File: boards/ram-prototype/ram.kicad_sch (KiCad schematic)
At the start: 29 parts, among them J1 SRAM_Bus

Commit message: Fix a bunch of issues
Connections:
- net D0: now also R1.1; no longer R4.1
- net D1: now also R2.1; no longer R5.1
- net D2: now also R3.1; no longer R6.1
- net D3: now also R4.1; no longer R7.1
- net D4: now also R5.1; no longer R8.1
- net D5: now also R6.1; no longer R9.1
- net D6: now also R7.1; no longer R10.1
- net D7: now also R8.1; no longer R11.1
- net GND: now also D11.2 (A), D14.2 (A), R11.2, R14.2
- net A0 renamed Address Decoder/A0
- net Address Decoder/A0: now also R9.1; no longer R1.1
- net A1 renamed Address Decoder/A1
- net Address Decoder/A1: now also R10.1; no longer R2.1
- net A2 renamed Address Decoder/A2
- net Address Decoder/A2: now also R11.1; no longer R3.1
- net nCE renamed Control Logic/nCE
- net nOE renamed Control Logic/nOE
- net nWE renamed Control Logic/nWE

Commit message: Clean up root
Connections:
- net D0: now also R4.1; no longer R1.1
- net D1: now also R5.1; no longer R2.1
- net D2: now also R6.1; no longer R3.1
- net D3: now also R7.1; no longer R4.1
- net D4: now also R8.1; no longer R5.1
- net D5: now also R9.1; no longer R6.1
- net D6: now also R10.1; no longer R7.1
- net D7: now also R11.1; no longer R8.1
- net GND: no longer D11.2 (A), D14.2 (A), R11.2, R14.2
- net Address Decoder/A0 renamed A0
- net A0: now also R1.1; no longer R9.1
- net Address Decoder/A1 renamed A1
- net A1: now also R2.1; no longer R10.1
- net Address Decoder/A2 renamed A2
- net A2: now also R3.1; no longer R11.1
- net Control Logic/nCE renamed nCE
- net Control Logic/nOE renamed nOE
- net Control Logic/nWE renamed nWE
- new net: D11.2 (A), R11.2
- new net: D14.2 (A), R14.2

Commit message: Continue with updates
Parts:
- removed J1: SRAM_Bus, symbol Connector_Generic:Conn_01x14
- added J1: SRAM_Bus, symbol Connector_Generic:Conn_01x16
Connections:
- net A0: now also J1.1 (Pin_1)
- net A1: now also J1.2 (Pin_2)
- net A2: now also J1.3 (Pin_3)
- net D0: now also J1.4 (Pin_4)
- net D1: now also J1.5 (Pin_5)
- net D2: now also J1.6 (Pin_6)
- net D3: now also J1.7 (Pin_7)
- net D4: now also J1.8 (Pin_8)
- net D5: now also J1.9 (Pin_9)
- net D6: now also J1.10 (Pin_10)
- net D7: now also J1.11 (Pin_11)
- net GND: now also J1.16 (Pin_16)
- net nCE: now also J1.12 (Pin_12)
- net nOE: now also J1.13 (Pin_13)
- net nWE: now also J1.14 (Pin_14)
- new net VCC: J1.15 (Pin_15)

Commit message: More reasonable top level designrout
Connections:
- net A0: now also J1.2 (Pin_2); no longer J1.1 (Pin_1)
- net A1: now also J1.3 (Pin_3); no longer J1.2 (Pin_2)
- net A2: now also J1.4 (Pin_4); no longer J1.3 (Pin_3)
- net D0: now also J1.5 (Pin_5); no longer J1.4 (Pin_4)
- net D1: now also J1.6 (Pin_6); no longer J1.5 (Pin_5)
- net D2: now also J1.7 (Pin_7); no longer J1.6 (Pin_6)
- net D3: now also J1.8 (Pin_8); no longer J1.7 (Pin_7)
- net D4: now also J1.9 (Pin_9); no longer J1.8 (Pin_8)
- net D5: now also J1.10 (Pin_10); no longer J1.9 (Pin_9)
- net D6: now also J1.11 (Pin_11); no longer J1.10 (Pin_10)
- net D7: now also J1.12 (Pin_12); no longer J1.11 (Pin_11)
- net GND: now also J1.1 (Pin_1); no longer J1.16 (Pin_16)
- net VCC: now also J1.16 (Pin_16); no longer J1.15 (Pin_15)
- net nCE: now also J1.13 (Pin_13); no longer J1.12 (Pin_12)
- net nOE: now also J1.14 (Pin_14); no longer J1.13 (Pin_13)
- net nWE: now also J1.15 (Pin_15); no longer J1.14 (Pin_14)

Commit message: Clean up root more and add more data
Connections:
- net A0: now also R14.1; no longer R1.1
- net A1: now also R13.1; no longer R2.1
- net A2: now also R12.1; no longer R3.1
- net D0: now also R11.1; no longer R4.1
- net D1: now also R10.1; no longer R5.1
- net D2: now also R9.1; no longer R6.1
- net D3: now also R8.1; no longer R7.1
- net D4: now also R7.1; no longer R8.1
- net D5: now also R6.1; no longer R9.1
- net D6: now also R5.1; no longer R10.1
- net D7: now also R4.1; no longer R11.1
- net nCE: now also R3.1; no longer R12.1
- net nOE: now also R2.1; no longer R13.1
- net nWE: now also R1.1; no longer R14.1

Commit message: fixup root page
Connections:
- net A0 is gone; now on net D7: J1.2 (Pin_2), R14.1
- net A1 is gone; now on net D6: J1.3 (Pin_3), R13.1
- net A2 is gone; now on net D5: J1.4 (Pin_4), R12.1
- net D0: now also J1.9 (Pin_9), R7.1; no longer J1.5 (Pin_5), R11.1
- net D1: now also J1.8 (Pin_8), R8.1; no longer J1.6 (Pin_6), R10.1
- net D3: now also J1.6 (Pin_6), R10.1; no longer J1.8 (Pin_8), R8.1
- net D4: now also J1.5 (Pin_5), R11.1; no longer J1.9 (Pin_9), R7.1
- net D5: no longer J1.10 (Pin_10), R6.1
- net D6: no longer J1.11 (Pin_11), R5.1
- net D7: no longer J1.12 (Pin_12), R4.1
- net nCE renamed Address Decoder/A2
- net nOE renamed Address Decoder/A1
- net nWE renamed Address Decoder/A0
- new net Control Logic/nCE: J1.12 (Pin_12), R4.1
- new net Control Logic/nOE: J1.11 (Pin_11), R5.1
- new net Control Logic/nWE: J1.10 (Pin_10), R6.1

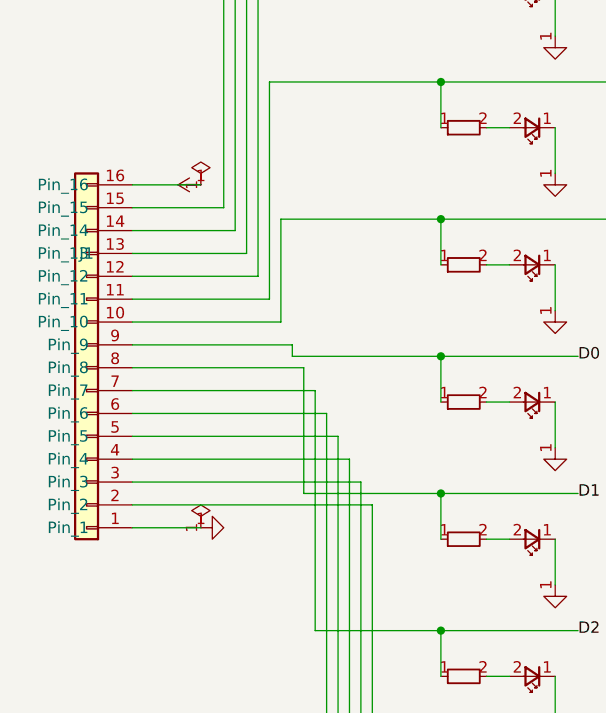
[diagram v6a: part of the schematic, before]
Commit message: add and fix some checks
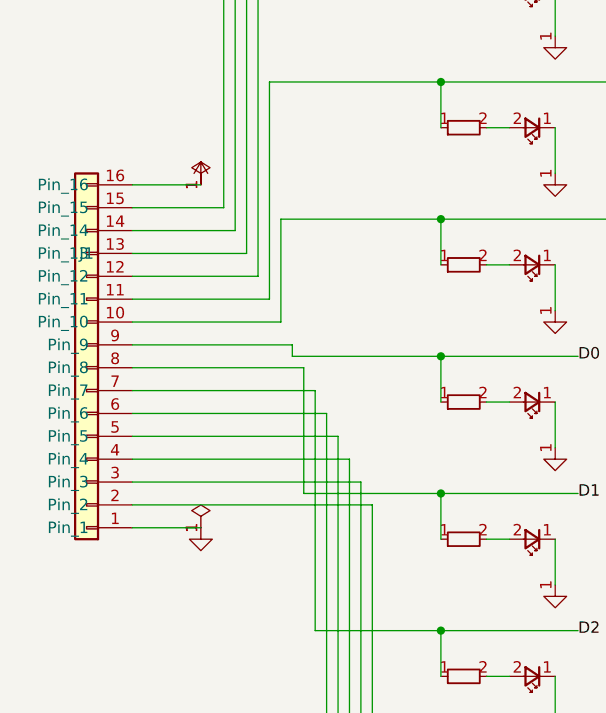
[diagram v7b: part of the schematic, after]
